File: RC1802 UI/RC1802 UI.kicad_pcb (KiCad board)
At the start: 2 copper layers, 99.1 x 80 mm, 47 parts, among them J1 Mount, J2 Mount, J3 Mount, J4 Mount, J6 CONN_02X20, SW1 RUN, SW10 IN5, SW11 IN6, SW12 IN7, SW2 IN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

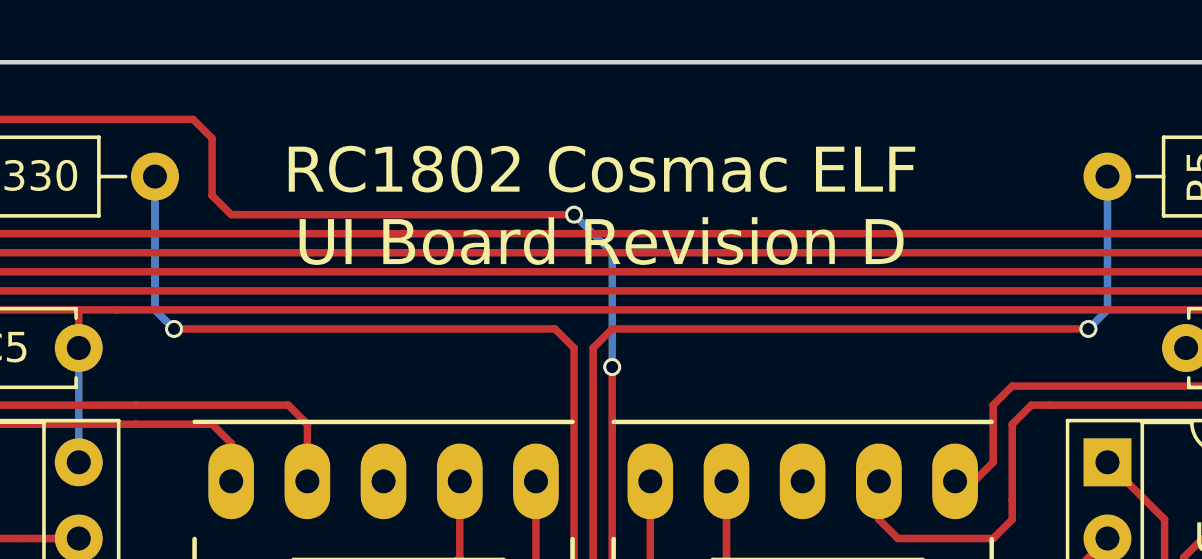
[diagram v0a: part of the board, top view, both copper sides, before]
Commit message: Forgot to regenerate filled zones, so wasted a PCB build :-(
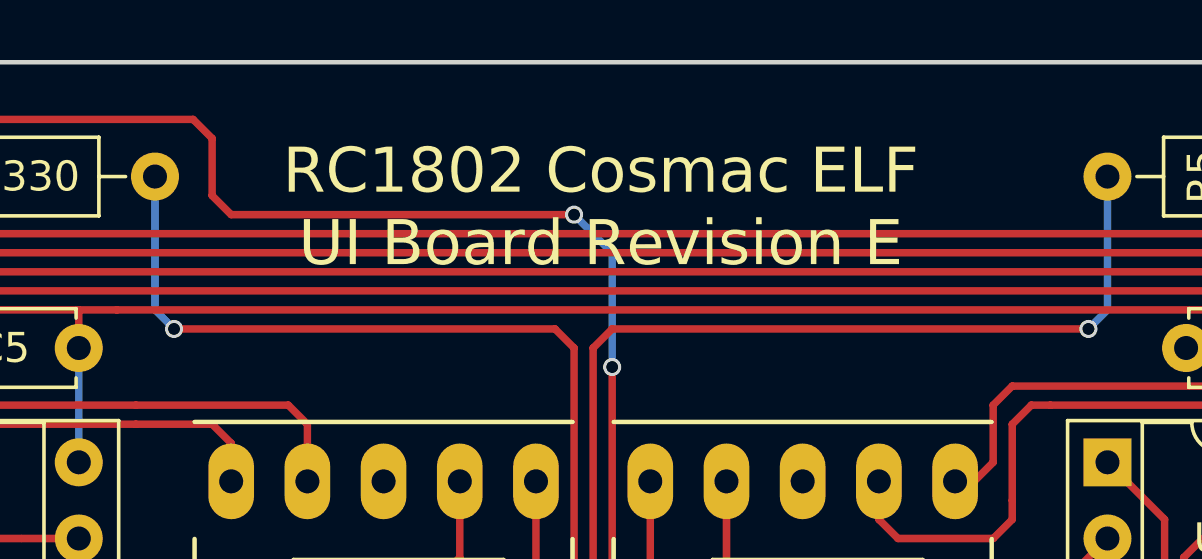
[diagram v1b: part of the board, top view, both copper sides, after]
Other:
- board text added: "RC1802 Cosmac ELF UI Board Revision E"
- board text removed: "RC1802 Cosmac ELF UI Board Revision D"
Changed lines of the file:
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@@
     (effects (font (size 1.5 1.5) (thickness 0.3)))
   )
-  (gr_text "RC1802 Cosmac ELF\nUI Board Revision D" (at 150.114 72.136) (layer F.SilkS)
+  (gr_text "RC1802 Cosmac ELF\nUI Board Revision E" (at 150.114 72.136) (layer F.SilkS)
     (effects (font (size 1.5 1.5) (thickness 0.3)))
   )
@@
   (segment (start 152.4 85.725) (end 167.005 85.725) (width 0.25) (layer F.Cu) (net 15))
   (segment (start 151.765 85.09) (end 152.4 85.725) (width 0.25) (layer F.Cu) (net 15))
-  (segment (start 125.73 117.53) (end 128.85 117.53) (width 0.25) (layer F.Cu) (net 16) (status 400000))
-  (segment (start 128.85 117.53) (end 132.715 113.665) (width 0.25) (layer F.Cu) (net 16) (status 800000))
-  (segment (start 132.715 113.665) (end 133.35 113.665) (width 0.25) (layer F.Cu) (net 16) (status C00000))
+  (segment (start 125.73 117.53) (end 128.85 117.53) (width 0.25) (layer F.Cu) (net 16))
+  (segment (start 128.85 117.53) (end 132.715 113.665) (width 0.25) (layer F.Cu) (net 16))
+  (segment (start 132.715 113.665) (end 133.35 113.665) (width 0.25) (layer F.Cu) (net 16))
   (segment (start 143.51 108.585) (end 134.62 108.585) (width 0.25) (layer F.Cu) (net 16))
-  (segment (start 134.62 108.585) (end 133.35 109.855) (width 0.25) (layer F.Cu) (net 16) (status 800000))
+  (segment (start 134.62 108.585) (end 133.35 109.855) (width 0.25) (layer F.Cu) (net 16))
   (segment (start 121.285 113.03) (end 121.285 113.085) (width 0.25) (layer B.Cu) (net 16))
-  (segment (start 121.285 113.085) (end 125.73 117.53) (width 0.25) (layer B.Cu) (net 16) (status 800000))
+  (segment (start 121.285 113.085) (end 125.73 117.53) (width 0.25) (layer B.Cu) (net 16))
   (segment (start 114.935 130.175) (end 111.76 130.175) (width 0.25) (layer F.Cu) (net 16))
   (via (at 107.95 133.985) (size 0.6) (drill 0.4) (layers F.Cu B.Cu) (net 16))
@@
   (segment (start 170.815 118.11) (end 170.815 120.65) (width 0.25) (layer F.Cu) (net 24))
   (segment (start 163.195 118.745) (end 164.465 117.475) (width 0.25) (layer F.Cu) (net 24))
-  (segment (start 129.54 115.57) (end 127 113.03) (width 0.25) (layer F.Cu) (net 24) (status 800000))
+  (segment (start 129.54 115.57) (end 127 113.03) (width 0.25) (layer F.Cu) (net 24))
   (via (at 129.54 115.57) (size 0.6) (drill 0.4) (layers F.Cu B.Cu) (net 24))
   (segment (start 133.35 119.38) (end 129.54 115.57) (width 0.25) (layer B.Cu) (net 24))
-  (segment (start 127 113.03) (end 125.73 113.03) (width 0.25) (layer F.Cu) (net 24) (status C00000))
-  (segment (start 125.73 113.03) (end 123.825 113.03) (width 0.25) (layer B.Cu) (net 24) (status 400000))
+  (segment (start 127 113.03) (end 125.73 113.03) (width 0.25) (layer F.Cu) (net 24))
+  (segment (start 125.73 113.03) (end 123.825 113.03) (width 0.25) (layer B.Cu) (net 24))
   (segment (start 114.935 111.125) (end 114.3 110.49) (width 0.25) (layer F.Cu) (net 24))
   (segment (start 115.57 111.125) (end 114.935 111.125) (width 0.25) (layer F.Cu) (net 24))

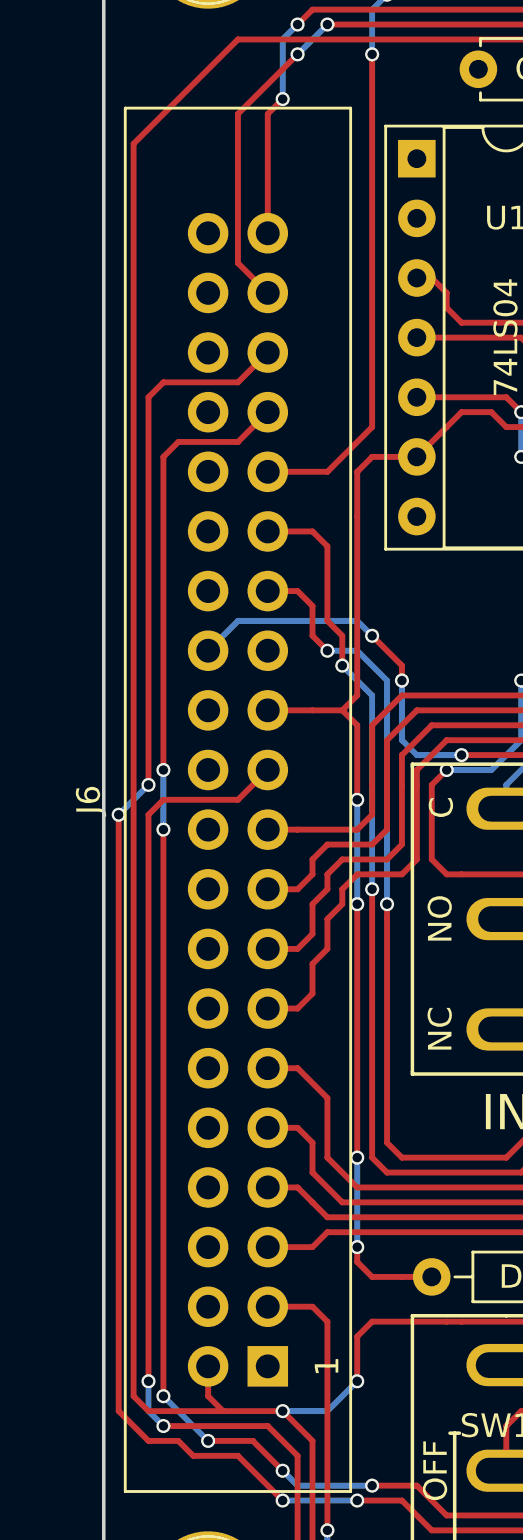
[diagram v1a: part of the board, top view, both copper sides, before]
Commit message: Changed UI connector
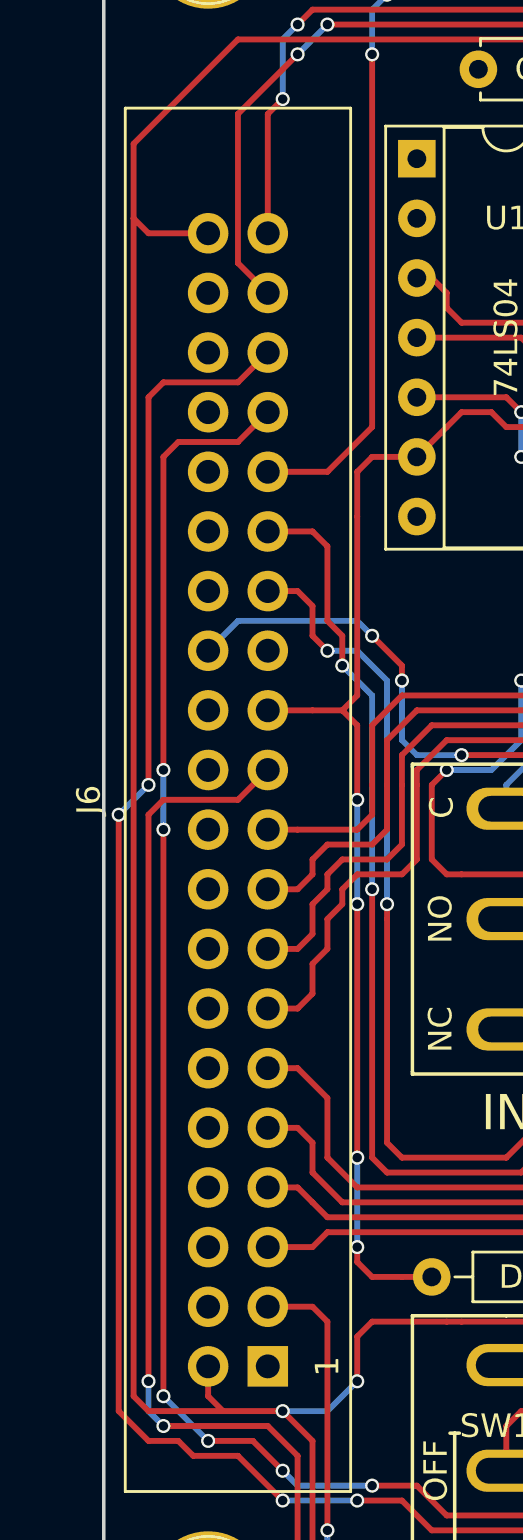
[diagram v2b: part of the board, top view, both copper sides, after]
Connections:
- J6 pad 40: GND -> VCC
- J6 pad 8: GND -> (no net)
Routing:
- net VCC: track 401.2 -> 404.6 mm

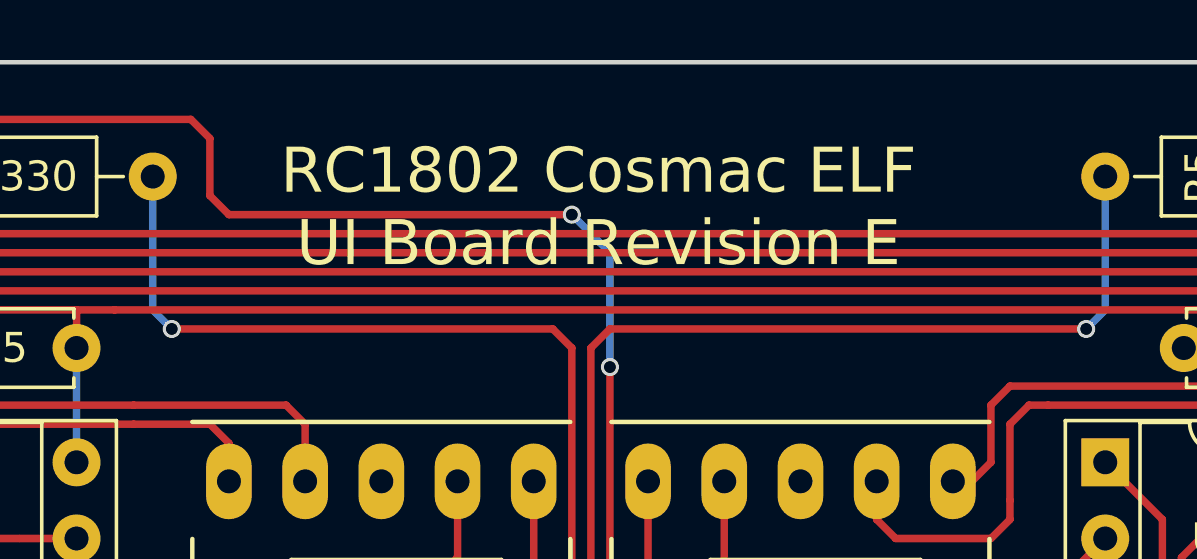
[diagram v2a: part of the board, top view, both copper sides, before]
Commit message: KiCad 5 update, both boards now marked F to match (without any actual changes)
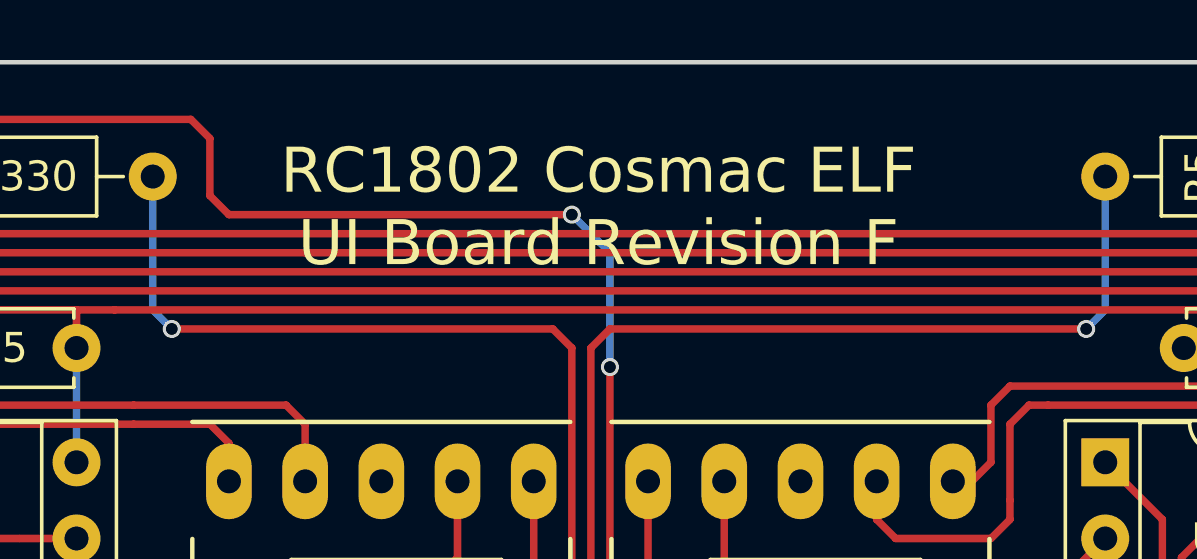
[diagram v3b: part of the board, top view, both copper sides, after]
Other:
- board text added: "RC1802 Cosmac ELF UI Board Revision F"
- board text added: "github.com/tebl"
- board text removed: "RC1802 Cosmac ELF UI Board Revision E"
- board text removed: "https://hvetebolle.blogspot.com"
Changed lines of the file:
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@@
-(kicad_pcb (version 4) (host pcbnew 4.0.7)
+(kicad_pcb (version 20171130) (host pcbnew "(5.1.5)-3")
   (general
-    (links 156)
-    (no_connects 0)
-    (area 95.375714 67.234999 204.344286 147.395001)
     (thickness 1.6)
     (drawings 29)
@@
     (zone_45_only no)
     (trace_min 0.2)
-    (segment_width 0.2)
-    (edge_width 0.15)
     (via_size 0.6)
     (via_drill 0.4)
@@
     (uvia_min_size 0.2)
     (uvia_min_drill 0.1)
+    (edge_width 0.15)
+    (segment_width 0.2)
     (pcb_text_width 0.3)
     (pcb_text_size 1.5 1.5)
-    (mod_edge_width 0.15)
+    (mod_edge_width 0.2)
     (mod_text_size 1 1)
     (mod_text_width 0.15)
@@
     (visible_elements 7FFFFFFF)
     (pcbplotparams
-      (layerselection 0x011fc_80000001)
+      (layerselection 0x011fc_ffffffff)
       (usegerberextensions true)
+      (usegerberattributes false)
+      (usegerberadvancedattributes false)
+      (creategerberjobfile false)
       (excludeedgelayer true)
       (linewidth 0.100000)
@@
       (hpglpennumber 1)
       (hpglpenspeed 20)
-      (hpglpendiameter 15)
-      (hpglpenoverlay 2)
+      (hpglpendiameter 15.000000)
       (psnegative false)
       (psa4output false)
@@
       (drillshape 0)
       (scaleselection 1)
-      (outputdirectory export/))
+      (outputdirectory "export/"))
   )
   (net 0 "")
@@
     (descr "Resistor, Axial_DIN0207 series, Axial, Horizontal, pin pitch=10.16mm, 0.25W = 1/4W, length*diameter=6.3*2.5mm^2, http://cdn-reichelt.de/documents/datenblatt/B400/1_4W%23YAG.pdf")
     (tags "Resistor Axial_DIN0207 series Axial Horizontal pin pitch 10.16mm 0.25W = 1/4W length 6.3mm diameter 2.5mm")
-    (fp_text reference R1 (at 6.985 0 360) (layer F.SilkS)
+    (fp_text reference R1 (at 6.985 0) (layer F.SilkS)
       (effects (font (size 1 1) (thickness 0.15)))
     )
@@
     (descr "D, DO-35_SOD27 series, Axial, Horizontal, pin pitch=7.62mm, , length*diameter=4*2mm^2, , http://www.diodes.com/_files/packages/DO-35.pdf")
     (tags "D DO-35_SOD27 series Axial Horizontal pin pitch 7.62mm  length 4mm diameter 2mm")
-    (fp_text reference D7 (at 3.81 0 360) (layer F.SilkS)
+    (fp_text reference D7 (at 3.81 0) (layer F.SilkS)
       (effects (font (size 1 1) (thickness 0.15)))
     )
@@
       (effects (font (size 1 1) (thickness 0.15)))
     )
-    (fp_text user %R (at 3.81 0 360) (layer F.Fab)
+    (fp_text user %R (at 3.81 0) (layer F.Fab)
       (effects (font (size 1 1) (thickness 0.15)))
     )
@@
     (descr "D, DO-35_SOD27 series, Axial, Horizontal, pin pitch=7.62mm, , length*diameter=4*2mm^2, , http://www.diodes.com/_files/packages/DO-35.pdf")
     (tags "D DO-35_SOD27 series Axial Horizontal pin pitch 7.62mm  length 4mm diameter 2mm")
-    (fp_text reference D3 (at 3.81 0 360) (layer F.SilkS)
+    (fp_text reference D3 (at 3.81 0) (layer F.SilkS)
       (effects (font (size 1 1) (thickness 0.15)))
     )
@@
       (effects (font (size 1 1) (thickness 0.15)))
     )
-    (fp_text user %R (at 3.81 0 360) (layer F.Fab)
+    (fp_text user %R (at 3.81 0) (layer F.Fab)
       (effects (font (size 1 1) (thickness 0.15)))
     )
@@
     (descr "D, DO-35_SOD27 series, Axial, Horizontal, pin pitch=7.62mm, , length*diameter=4*2mm^2, , http://www.diodes.com/_files/packages/DO-35.pdf")
     (tags "D DO-35_SOD27 series Axial Horizontal pin pitch 7.62mm  length 4mm diameter 2mm")
-    (fp_text reference D2 (at 3.81 0 360) (layer F.SilkS)
+    (fp_text reference D2 (at 3.81 0) (layer F.SilkS)
       (effects (font (size 1 1) (thickness 0.15)))
     )
@@
       (effects (font (size 1 1) (thickness 0.15)))
     )
-    (fp_text user %R (at 3.81 0 360) (layer F.Fab)
+    (fp_text user %R (at 3.81 0) (layer F.Fab)
       (effects (font (size 1 1) (thickness 0.15)))
     )
@@
     (descr "C, Disc series, Radial, pin pitch=5.00mm, , diameter*width=4.7*2.5mm^2, Capacitor, http://www.vishay.com/docs/45233/krseries.pdf")
     (tags "C Disc series Radial pin pitch 5.00mm  diameter 4.7mm width 2.5mm Capacitor")
-    (fp_text reference C3 (at 2.54 0 360) (layer F.SilkS)
+    (fp_text reference C3 (at 2.54 0) (layer F.SilkS)
       (effects (font (size 1 1) (thickness 0.15)))
     )
@@
     (fp_line (start 6.05 1.6) (end 6.05 -1.6) (layer F.CrtYd) (width 0.05))
     (fp_line (start 6.05 -1.6) (end -1.05 -1.6) (layer F.CrtYd) (width 0.05))
-    (fp_text user %R (at 2.5 0 360) (layer F.Fab)
+    (fp_text user %R (at 2.5 0) (layer F.Fab)
       (effects (font (size 1 1) (thickness 0.15)))
     )
@@
       (effects (font (size 1 1) (thickness 0.15)))
     )
-    (fp_text value DP_STROBE (at -2.54 1.27 360) (layer F.SilkS)
+    (fp_text value DP_STROBE (at -2.54 1.27) (layer F.SilkS)
       (effects (font (size 1 1) (thickness 0.15)))
     )
@@
     (fp_line (start 1.8 4.35) (end 1.8 -1.8) (layer F.CrtYd) (width 0.05))
     (fp_line (start 1.8 -1.8) (end -1.8 -1.8) (layer F.CrtYd) (width 0.05))
-    (fp_text user %R (at 0 1.27 360) (layer F.Fab)
+    (fp_text user %R (at 0 1.27) (layer F.Fab)
       (effects (font (size 1 1) (thickness 0.15)))
     )
@@
   (module switches:SPDT_SWITCH (layer F.Cu)
     (at 186.055 113.03 270)
-    (fp_text reference SW3 (at 2.54 0 360) (layer F.SilkS) hide
-      (effects (font (size 1 1) (thickness 0.15)))
-    )
-    (fp_text value MP (at -2.54 0 360) (layer F.Fab) hide
+    (fp_text reference SW3 (at 2.54 0) (layer F.SilkS) hide
+      (effects (font (size 1 1) (thickness 0.15)))
+    )
+    (fp_text value MP (at -2.54 0) (layer F.Fab) hide
       (effects (font (size 1 1) (thickness 0.15)))
     )
@@
   (module switches:SPDT_SWITCH (layer F.Cu)
     (at 117.475 136.525 270)
-    (fp_text reference SW12 (at -1.905 0 360) (layer F.SilkS)
-      (effects (font (size 1 1) (thickness 0.15)))
-    )
-    (fp_text value IN7 (at 2.54 0 360) (layer F.Fab)
+    (fp_text reference SW12 (at -1.905 0) (layer F.SilkS)
+      (effects (font (size 1 1) (thickness 0.15)))
+    )
+    (fp_text value IN7 (at 2.54 0) (layer F.Fab)
       (effects (font (size 1 1) (thickness 0.15)))
     )
@@
   (module switches:SPDT_SWITCH (layer F.Cu)
     (at 126.365 136.525 270)
-    (fp_text reference SW11 (at -1.905 0 360) (layer F.SilkS)
-      (effects (font (size 1 1) (thickness 0.15)))
-    )
-    (fp_text value IN6 (at 2.54 0 360) (layer F.Fab)
+    (fp_text reference SW11 (at -1.905 0) (layer F.SilkS)
+      (effects (font (size 1 1) (thickness 0.15)))
+    )
+    (fp_text value IN6 (at 2.54 0) (layer F.Fab)
       (effects (font (size 1 1) (thickness 0.15)))
     )
@@
   (module switches:SPDT_SWITCH (layer F.Cu)
     (at 135.255 136.525 270)
-    (fp_text reference SW10 (at -1.905 0 360) (layer F.SilkS)
-      (effects (font (size 1 1) (thickness 0.15)))
-    )
-    (fp_text value IN5 (at 2.54 0 360) (layer F.Fab)
+    (fp_text reference SW10 (at -1.905 0) (layer F.SilkS)
+      (effects (font (size 1 1) (thickness 0.15)))
+    )
+    (fp_text value IN5 (at 2.54 0) (layer F.Fab)
       (effects (font (size 1 1) (thickness 0.15)))
     )
@@
   (module switches:SPDT_SWITCH (layer F.Cu)
     (at 144.145 136.525 270)
-    (fp_text reference SW9 (at -1.905 0 360) (layer F.SilkS)
-      (effects (font (size 1 1) (thickness 0.15)))
-    )
-    (fp_text value IN4 (at 2.54 0 360) (layer F.Fab)
+    (fp_text reference SW9 (at -1.905 0) (layer F.SilkS)
+      (effects (font (size 1 1) (thickness 0.15)))
+    )
+    (fp_text value IN4 (at 2.54 0) (layer F.Fab)
       (effects (font (size 1 1) (thickness 0.15)))
     )
@@
   (module switches:SPDT_SWITCH (layer F.Cu)
     (at 155.575 136.525 270)
-    (fp_text reference SW8 (at -1.905 0 360) (layer F.SilkS)
-      (effects (font (size 1 1) (thickness 0.15)))
-    )
-    (fp_text value IN3 (at 2.54 0 360) (layer F.Fab)
+    (fp_text reference SW8 (at -1.905 0) (layer F.SilkS)
+      (effects (font (size 1 1) (thickness 0.15)))
+    )
+    (fp_text value IN3 (at 2.54 0) (layer F.Fab)
       (effects (font (size 1 1) (thickness 0.15)))
     )
@@
   (module switches:SPDT_SWITCH (layer F.Cu)
     (at 164.465 136.525 270)
-    (fp_text reference SW7 (at -1.905 0 360) (layer F.SilkS)
-      (effects (font (size 1 1) (thickness 0.15)))
-    )
-    (fp_text value IN2 (at 2.54 0 360) (layer F.Fab)
+    (fp_text reference SW7 (at -1.905 0) (layer F.SilkS)
+      (effects (font (size 1 1) (thickness 0.15)))
+    )
+    (fp_text value IN2 (at 2.54 0) (layer F.Fab)
       (effects (font (size 1 1) (thickness 0.15)))
     )
@@
   (module switches:SPDT_SWITCH (layer F.Cu)
     (at 182.245 136.525 270)
-    (fp_text reference SW5 (at -1.905 0 360) (layer F.SilkS)
-      (effects (font (size 1 1) (thickness 0.15)))
-    )
-    (fp_text value IN0 (at 2.54 0 360) (layer F.Fab)
+    (fp_text reference SW5 (at -1.905 0) (layer F.SilkS)
+      (effects (font (size 1 1) (thickness 0.15)))
+    )
+    (fp_text value IN0 (at 2.54 0) (layer F.Fab)
       (effects (font (size 1 1) (thickness 0.15)))
     )
@@
   (module switches:SPDT_PUSH (layer F.Cu)
     (at 117.475 113.03 270)
-    (fp_text reference SW2 (at 2.54 0 360) (layer F.SilkS) hide
-      (effects (font (size 1 1) (thickness 0.15)))
-    )
-    (fp_text value IN (at -2.54 0 540) (layer F.Fab) hide
+    (fp_text reference SW2 (at 2.54 0) (layer F.SilkS) hide
+      (effects (font (size 1 1) (thickness 0.15)))
+    )
+    (fp_text value IN (at -2.54 0 180) (layer F.Fab) hide
       (effects (font (size 1 1) (thickness 0.15)))
     )
@@
     (effects (font (size 1.5 1.5) (thickness 0.3)))
   )
-  (gr_text https://hvetebolle.blogspot.com (at 149.86 145.415) (layer B.SilkS)
+  (gr_text github.com/tebl (at 149.86 145.415) (layer B.SilkS)
     (effects (font (size 1.5 1.5) (thickness 0.3)) (justify mirror))
   )
@@
     (effects (font (size 1.5 1.5) (thickness 0.3)))
   )
-  (gr_text "RC1802 Cosmac ELF\nUI Board Revision E" (at 150.114 72.136) (layer F.SilkS)
+  (gr_text "RC1802 Cosmac ELF\nUI Board Revision F" (at 150.114 72.136) (layer F.SilkS)
     (effects (font (size 1.5 1.5) (thickness 0.3)))
   )
